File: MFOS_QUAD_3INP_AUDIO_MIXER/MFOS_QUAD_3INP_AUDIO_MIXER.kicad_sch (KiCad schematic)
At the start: 140 parts, among them J1 Jack-DC, J10 Jack-DC, J11 Jack-DC, J12 Jack-DC, J13 Jack-DC, J14 Jack-DC, J15 Jack-DC, J16 Jack-DC, J17 Conn_01x01, J18 Conn_01x01, J19 Conn_01x01, J2 Jack-DC, J20 Conn_01x01, J21 Conn_01x01, J22 Conn_01x01, J23 Conn_01x01, J24 Conn_01x01, J25 Conn_01x01, J26 Conn_01x01, J27 Conn_01x01, J28 Conn_01x01, J29 Conn_01x01, J3 Jack-DC, J30 Conn_01x01, J31 Conn_01x01, J32 Conn_01x01, J33 Conn_01x01, J34 Conn_01x01, J35 Conn_01x01, J36 Conn_01x01, J37 Conn_01x01, J38 Conn_01x01, J39 Conn_01x01, J4 Jack-DC, J40 Conn_01x01, J41 Conn_01x01, J42 Conn_01x01, J43 Conn_01x01, J44 Conn_01x01, J5 Jack-DC, J6 Jack-DC, J7 Jack-DC, J8 Jack-DC, J9 Jack-DC, U1 TL074, U2 TL074, U3 TL074, U4 TL074

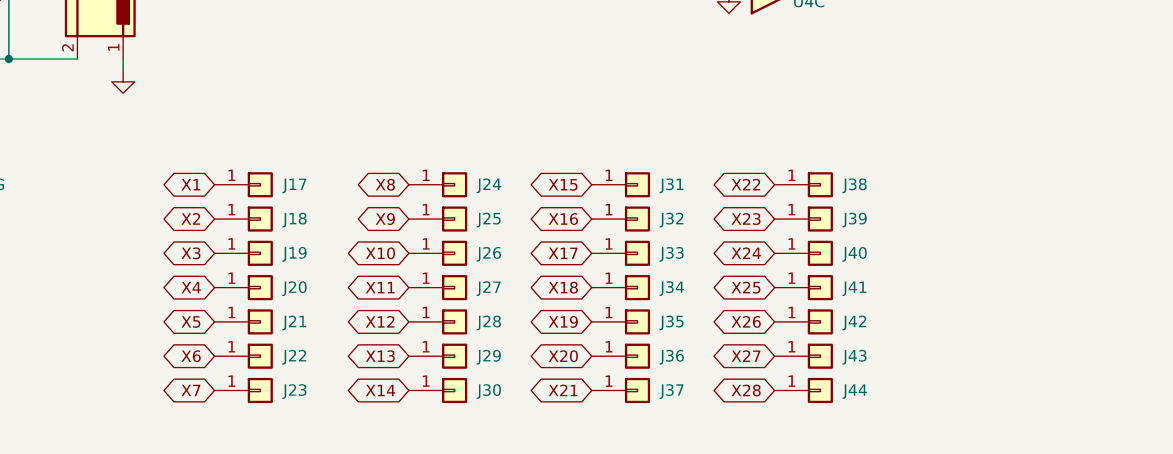
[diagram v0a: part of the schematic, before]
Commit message: Excluded some parts from board
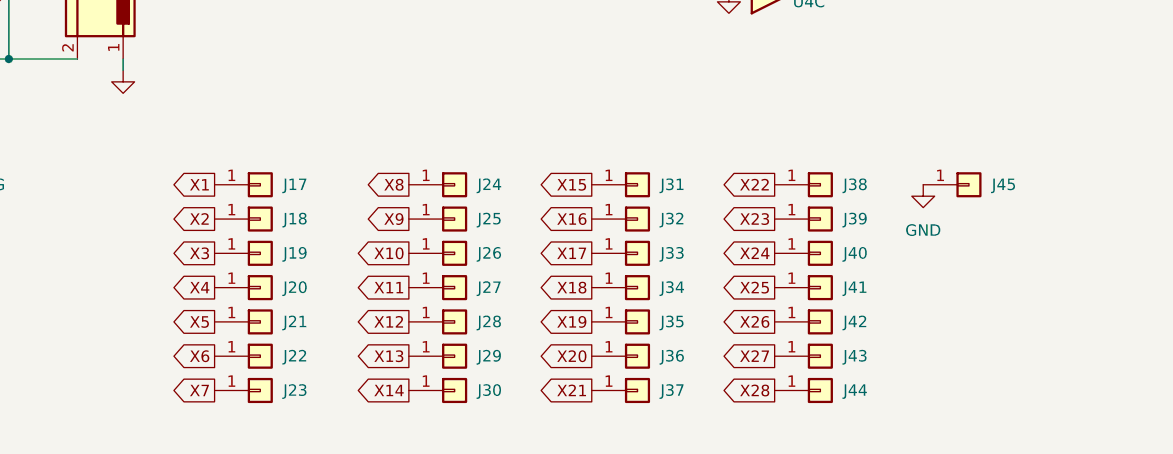
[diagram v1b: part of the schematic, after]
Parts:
- added J45: Conn_01x01, symbol Connector_Generic:Conn_01x01
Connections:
- net GND: now also J45.1 (Pin_1)

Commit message: Revision until and with audio mixer complete
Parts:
- removed C1, C2, C3, C5, C7: 1uF, symbol Device:C
- removed C10, C19, C20, C9: 10uF, symbol Device:C
- added C1, C2, C3, C5, C7: 1uF, symbol dhk:C_Alu_Bipolar
- added C10, C19, C20, C9: 10uF, symbol dhk:C_Alu_Bipolar
- C12, C13, C15, C17, C18, C8: symbol Device:C -> dhk:C_Alu_Bipolar
- J17, J18, J19, J20, J21, J22, J23, J24, J25, J26, J27, J28, J29, J30, J31, J32, J33, J34, J35, J36, J37, J38, J39, J40, J41, J42, J43, J44, J45: now left out of the parts list
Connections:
- net X12: now also C9.1
- net X14: now also C10.1
- net X26: now also C20.1
- net X27: now also C19.1
- net at R27.2, U1.8: now also C9.2
- net at R25.2, U2.8: now also C10.2
- net at J2.2: now also C2.2
- net at R55.2, U4.8: now also C20.2
- net at J3.2: now also C3.2
- net at R13.3: now also C3.1
- net at R16.3: now also C5.1
- net at J1.2: now also C1.2
- net at R1.3: now also C1.1
- net at J5.2: now also C7.2
- net at R21.3: now also C7.1
- net at R51.2, U3.8: now also C19.2
- net at R4.3: now also C2.1
- net at J4.2: now also C5.2

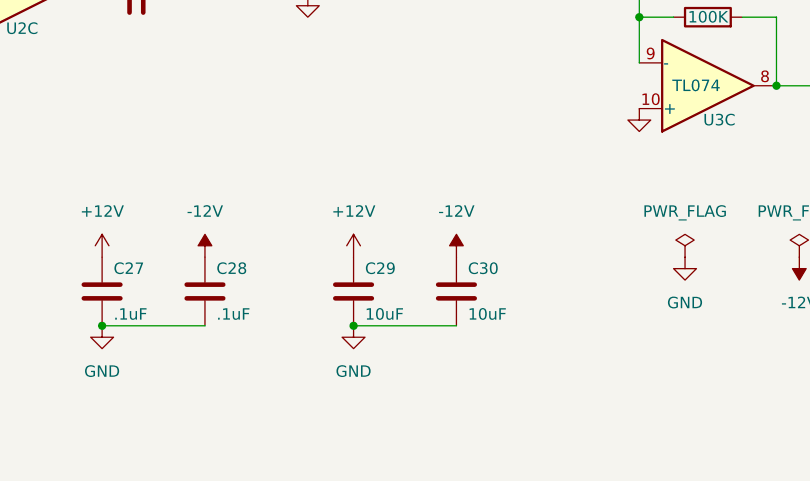
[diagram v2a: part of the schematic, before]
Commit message: Designs adapted for BOM
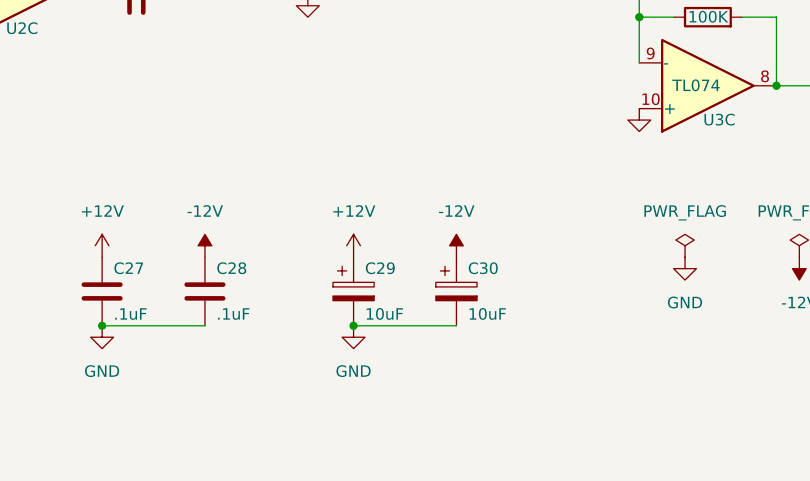
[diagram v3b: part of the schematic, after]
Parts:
- C29, C30: symbol Device:C -> Device:C_Polarized
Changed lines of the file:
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@@
     (pin "2")
   )
-  (symbol (lib_id "Device:C") (at 201.93 151.13 0) (unit 1)
+  (symbol (lib_id "Device:C_Polarized") (at 201.93 151.13 0) (unit 1)
     (in_bom yes) (on_board yes)
     (property "Reference" "C29" (id 0) (at 203.2 148.59 0)
@@
     (pin "1")
   )
-  (symbol (lib_id "Device:C") (at 213.36 151.13 0) (unit 1)
+  (symbol (lib_id "Device:C_Polarized") (at 213.36 151.13 0) (unit 1)
     (in_bom yes) (on_board yes)
     (property "Reference" "C30" (id 0) (at 214.63 148.59 0)
